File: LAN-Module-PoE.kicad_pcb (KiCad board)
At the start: 2 copper layers, 28.6 x 53.3 mm, 91 parts, among them J1 HY931147C, J10 ProtoCastellatedHeader, J11 ProtoCastellatedHeader, J12 ProtoCastellatedHeader, J13 ProtoCastellatedHeader, J14 ProtoCastellatedHeader, J15 ProtoCastellatedHeader, J16 ProtoCastellatedHeader, J17 ProtoCastellatedHeader, J18 ProtoCastellatedHeader, J19 ProtoCastellatedHeader, J20 ProtoCastellatedHeader, J21 ProtoCastellatedHeader, J22 ProtoCastellatedHeader, J23 ProtoCastellatedHeader, J24 ProtoCastellatedHeader, J25 ProtoCastellatedHeader, J26 ProtoCastellatedHeader, J27 ProtoCastellatedHeader, J28 ProtoCastellatedHeader, J3 ProtoCastellatedHeader, J4 ProtoCastellatedHeader, J5 ProtoCastellatedHeader, J6 ProtoCastellatedHeader, J7 ProtoCastellatedHeader, J8 ProtoCastellatedHeader, J9 ProtoCastellatedHeader, SW1 RESET, U1 ESP32-U4WDH, U2 Si3404, U3 LV2842XLVDDCR, U4 RTL8201F, Y1 40MHz ±10ppm

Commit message: Final revision of PoE variant
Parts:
- added C17: 100n, Capacitor_SMD:C_0603_1608Metric, F.Cu at (41.8, 43.8)
- added D3: Green, LED_SMD:LED_0603_1608Metric, F.Cu at (46.0, 27.5)
- added R26: 33k 1%, Resistor_SMD:R_0603_1608Metric, F.Cu at (39.5, 43.0)
- added R27: 10k 1%, Resistor_SMD:R_0603_1608Metric, F.Cu at (39.5, 44.2)
- added R28: 1k, Resistor_SMD:R_0603_1608Metric, F.Cu at (47.8, 27.5)
- J10, J11, J12, J13, J14, J15, J16, J17, J18, J19, J20, J21, J22, J23, J24, J25, J26, J27, J28, J3, J4, J5, J6, J7, J8, J9: footprint Visclib:ProtoCastellatedHeader_65mil -> Visclib:ProtoHeader_65mil
- L2: value 10uH -> 10uH 1A
- moved SW1 19.7 mm to (27.4, 27.4)
- moved L2 18.7 mm to (44.8, 43.8), turned to 0 degrees
- moved U3 17.1 mm to (40.8, 47.2), turned to -90 degrees
- moved D2 10.9 mm to (44.8, 47.0), turned to 0 degrees
- moved R5 10.1 mm to (26.2, 30.2), turned to 0 degrees
- moved R22 8.41 mm to (41.1, 27.1)
- moved C10 7.36 mm to (26.2, 33.5), turned to 180 degrees
- moved R24 6.50 mm to (37.5, 47.6)
- moved R4 5.13 mm to (42.7, 27.1), turned to -90 degrees
- moved R1 4.72 mm to (26.2, 32.0), turned to 0 degrees
- moved R23 4.37 mm to (37.5, 49.0), turned to 0 degrees
- moved C21 1.63 mm to (45.8, 40.8), turned to 180 degrees
- moved C12 0.50 mm to (40.2, 41.0)
- moved C13 0.25 mm to (43.2, 38.6)
- moved R2 0.20 mm to (30.6, 28.6)
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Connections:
- C1 pad 1: /VIN -> /12V
- C18 pad 1: /VIN -> /12V
- C27 pad 1: /VIN -> /12V
- C4 pad 1: /VIN -> /12V
- D1 pad 1: /VIN -> /12V
- D2 pad 1: unconnected-(D2-Pad1) -> Net-(C17-Pad2)
- D2 pad 2: unconnected-(D2-Pad2) -> GND
- J1 pad 9: /VIN -> /12V
- J1 pad SH: (no net) -> GND
- J15 pad 1: /3V3 -> +3V3
- J28 pad 1: /VIN -> /12V
- L2 pad 1: unconnected-(L2-Pad1) -> Net-(C17-Pad2)
- L2 pad 2: unconnected-(L2-Pad2) -> +3V3
- R19 pad 1: /VIN -> /12V
- R23 pad 2: /VIN -> /12V
- R6 pad 1: /VIN -> /12V
- U2 pad 13: /VIN -> /12V
- U3 pad 1: unconnected-(U3-Pad1) -> Net-(C17-Pad1)
- U3 pad 3: unconnected-(U3-Pad3) -> Net-(R26-Pad1)
- U3 pad 4: unconnected-(U3-Pad4) -> /12V
- U3 pad 5: unconnected-(U3-Pad5) -> /12V
- U3 pad 6: unconnected-(U3-Pad6) -> Net-(C17-Pad2)
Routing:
- net GND: track 116.9 -> 241.5 mm, vias 12 -> 22
- net /12V: track 0.00 -> 61.8 mm, vias 0 -> 2
- net /VIN: track 48.8 -> 0.00 mm, vias 2 -> 0
- net +3V3: track 51.6 -> 95.7 mm, vias 3 -> 5
- net /EN: track 9.56 -> 28.6 mm, vias 1 -> 2
- net /U0RXD: track 1.73 -> 14.0 mm, vias 0 -> 1
- net Net-(R22-Pad2): track 27.1 -> 15.0 mm
- net /BOOT: track 16.3 -> 23.9 mm
- net /POE_NEG: track 29.3 -> 21.8 mm
- net /U0TXD: track 1.76 -> 9.14 mm, vias 0 -> 1
- net Net-(C17-Pad2): track 0.00 -> 7.13 mm
- net /IO13: track 18.1 -> 24.2 mm, vias 1 -> 2
- net /ETH_RXD0: track 25.0 -> 30.9 mm
- net /IO16: track 18.4 -> 24.1 mm, vias 1 -> 2
- net /ETH_RXD1: track 24.4 -> 29.9 mm
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- added copper zone on F.Cu, net +3V3
- added copper zone on F.Cu, net /12V
- added copper zone on F.Cu, net /SWO
- added copper zone on B.Cu, net GND
- added copper zone on F.Cu, net GND
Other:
- board text added: "12V"
- board text added: "3.3V"
- board text added: "BOOT"
- board text added: "EN"
- board text added: "GND"
- board text added: "IO12"
- board text added: "IO13"
- board text added: "IO14"
- board text added: "IO15"
- board text added: "IO16"
- board text added: "IO2"
- board text added: "IO32"
- board text added: "IO33"
- board text added: "IO34"
- board text added: "IO35"
- board text added: "IO37"
- board text added: "IO38"
- board text added: "IO4"
- board text added: "IO5"
- board text added: "RX"
- board text added: "TX"
- board text added: "VN"
- board text added: "VP"

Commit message: Fix footprint for ESP32 (QFN 5x5), add heat pad for PoE regulator
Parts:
- C8: footprint Capacitor_SMD:C_0603_1608Metric -> Resistor_SMD:R_0603_1608Metric
- R23: value 10k -> 1k
- R24: value 10k -> 8.2k
- U1: footprint Visclib:ESP32-REDUCED -> Package_DFN_QFN:QFN-48-1EP_5x5mm_P0.35mm_EP3.7x3.7mm_ThermalVias
- moved L1 0.20 mm to (41.4, 33.6)
- moved C16 0.10 mm to (41.4, 35.1)
- moved U1 0.10 mm to (36.3, 32.0)
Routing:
- net Net-(R4-Pad2): track 18.7 -> 44.1 mm
- net Net-(R22-Pad2): track 15.0 -> 38.3 mm
- net +3V3: track 95.7 -> 104.3 mm, vias 5 -> 10
- net /ETH_RXD1: track 29.9 -> 25.2 mm
- net /IO15: track 22.4 -> 26.5 mm
- net /ETH_RXD0: track 30.9 -> 28.3 mm
- net /EN: track 28.6 -> 30.9 mm
- net /ETH_MDC: track 8.42 -> 10.2 mm, vias 0 -> 2
- net /IO4: track 28.1 -> 29.9 mm
- net /ETH_MDIO: track 9.18 -> 10.9 mm, vias 0 -> 2
- net /IO5: track 29.3 -> 30.8 mm
- net /IO14: track 34.7 -> 36.1 mm
- net /IO35: track 18.1 -> 19.3 mm
- net /IO32: track 16.1 -> 17.2 mm
- net /BOOT: track 23.9 -> 25.0 mm
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- added copper zone on B.Cu, net /POE_NEG
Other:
- board size 28.6 x 53.3 mm -> 28.6 x 53.8 mm

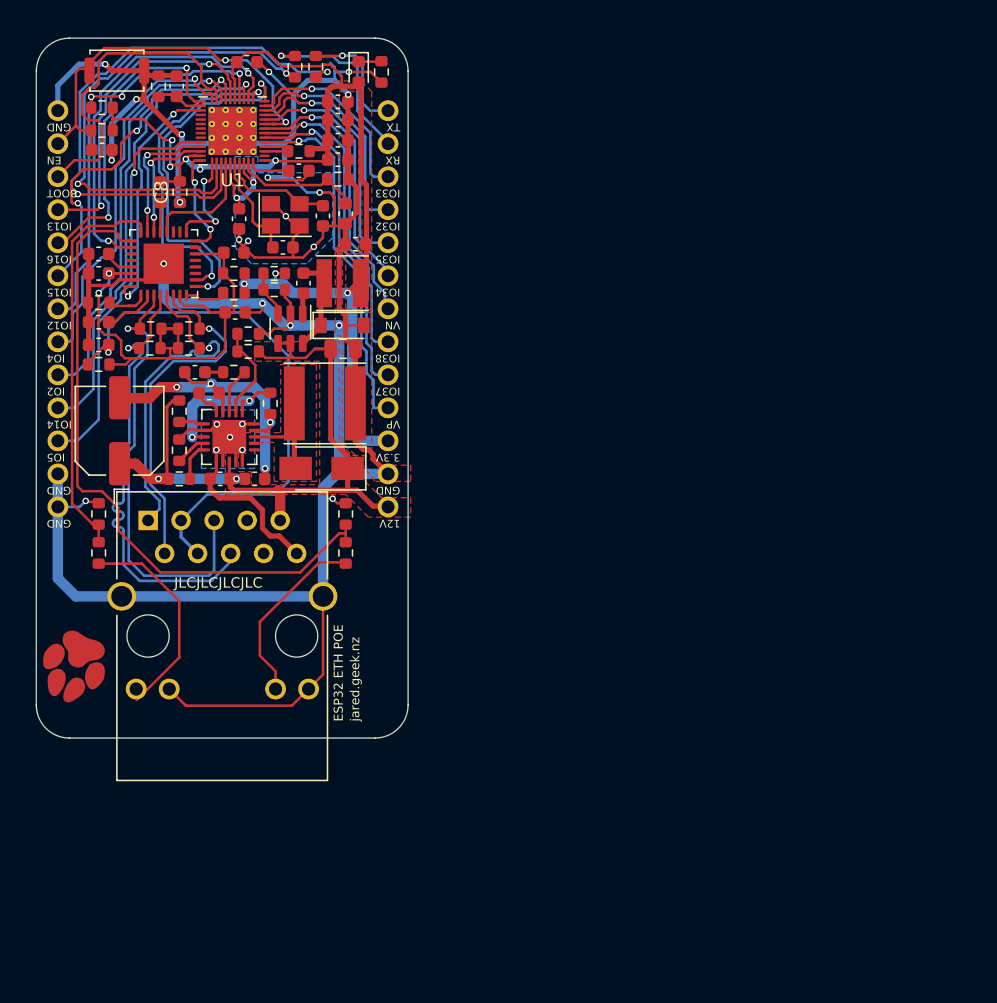
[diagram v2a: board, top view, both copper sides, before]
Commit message: Re-layout with narrower board outline (-0.1")
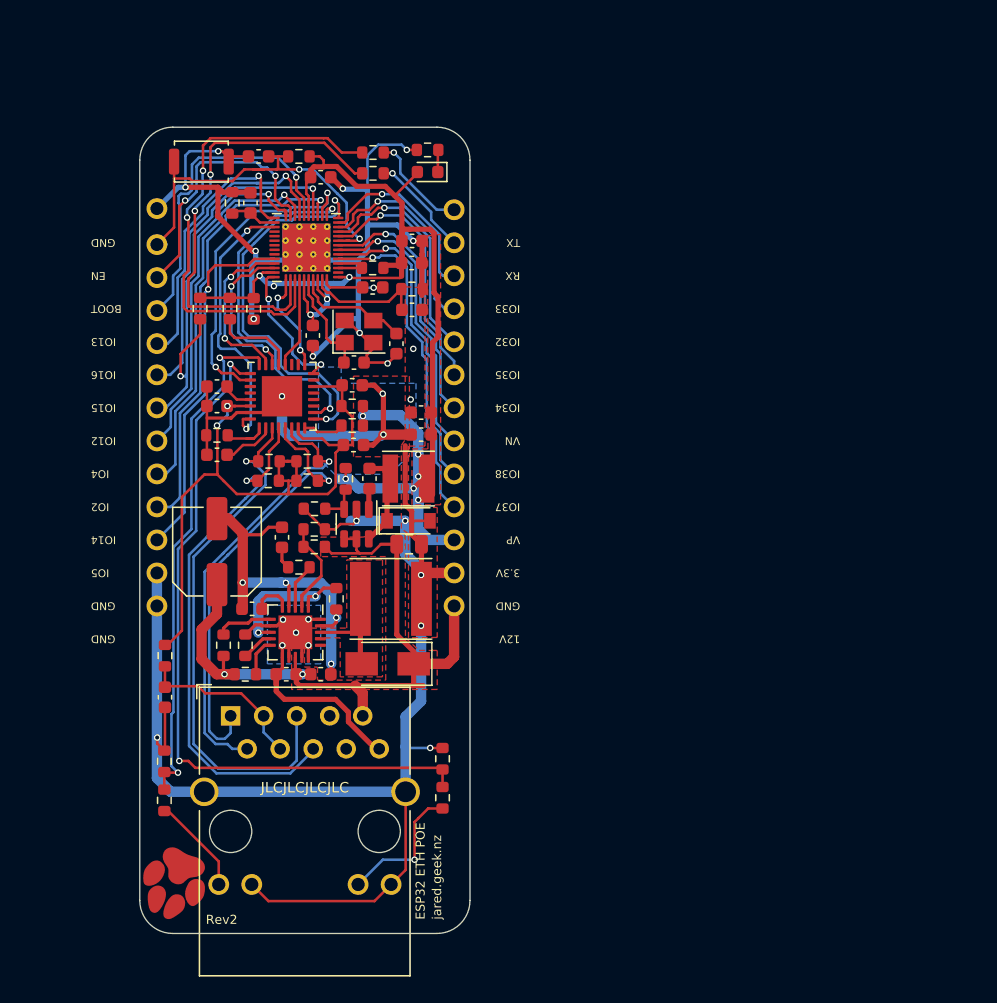
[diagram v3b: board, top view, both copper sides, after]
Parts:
- removed C7: 100n, Capacitor_SMD:C_0603_1608Metric
- moved C3 27.6 mm to (31.1, 75.6), turned to 90 degrees
- moved C5 23.4 mm to (50.8, 53.7), turned to 0 degrees
- moved R25 23.0 mm to (31.1, 72.4), turned to -90 degrees
- moved R11 20.3 mm to (52.5, 80.3)
- moved R16 20.3 mm to (52.5, 83.3)
- moved R12 19.7 mm to (31.1, 80.5)
- moved R15 19.7 mm to (31.1, 83.5)
- moved LOGO1 18.4 mm to (31.7, 90.2)
- moved R6 18.3 mm to (35.6, 71.6), turned to 90 degrees
- moved R5 17.2 mm to (33.8, 45.7), turned to 90 degrees
- moved R27 17.1 mm to (42.6, 61.1), turned to 0 degrees
- moved C20 16.9 mm to (37.8, 68.8), turned to 180 degrees
- moved R26 16.7 mm to (45.0, 58.8), turned to 90 degrees
- moved J1 16.3 mm to (36.1, 77.0)
- moved C1 15.9 mm to (40.4, 73.8)
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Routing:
- net /MDI0_CT: track 42.5 -> 12.9 mm, vias 1 -> 0
- net GND: track 242.0 -> 222.5 mm, vias 20 -> 22
- net /LAN_3P3V: track 41.0 -> 54.4 mm
- net /RTL_LED0: track 30.8 -> 39.9 mm, vias 0 -> 2
- net /ETH_LED0: track 16.4 -> 7.56 mm
- net /MDI1_P: track 26.4 -> 34.6 mm
- net /MDI1_N: track 27.2 -> 34.2 mm
- net Net-(R4-Pad2): track 44.1 -> 37.2 mm
- net /MDI0_P: track 34.6 -> 41.5 mm
- net /MDI0_N: track 35.7 -> 41.2 mm
- net /U0RXD: track 14.0 -> 8.58 mm
- net /RTL_LED1: track 50.6 -> 55.9 mm, vias 0 -> 2
- net /ETH_CRS_DV: track 29.7 -> 25.1 mm
- net /BOOT: track 25.0 -> 20.4 mm, vias 0 -> 2
- net /12V: track 61.8 -> 66.2 mm
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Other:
- board size 28.6 x 53.8 mm -> 25.4 x 62 mm
- board text added: "Rev2"
- board text removed: "USB-UART"

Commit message: Finalize layout for rev2
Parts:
- added C28: 1u, Capacitor_SMD:C_0603_1608Metric, F.Cu at (35.9, 64.4)
- added C7: 1u, Capacitor_SMD:C_0603_1608Metric, F.Cu at (34.4, 64.4)
- added J2: ProtoCastellatedHeader, Visclib:ProtoHeader_65mil, F.Cu at (53.3, 73.7)
- added J29: ProtoCastellatedHeader, Visclib:ProtoHeader_65mil, F.Cu at (53.3, 76.3)
- added L4: 10uH, Inductor_SMD:L_Taiyo-Yuden_NR-80xx, F.Cu at (62.0, 67.7)
- added R29: 50R, Resistor_SMD:R_0603_1608Metric, F.Cu at (45.5, 36.1)
- added R30: 50R, Resistor_SMD:R_0603_1608Metric, F.Cu at (44.0, 36.1)
- added R31: 50R, Resistor_SMD:R_0603_1608Metric, F.Cu at (35.1, 50.2)
- added R32: 50R, Resistor_SMD:R_0603_1608Metric, F.Cu at (37.2, 40.0)
- added TP1: TP, Visclib:TP-1MM, F.Cu at (39.9, 47.6)
- added TP2: TP, Visclib:TP-1MM, F.Cu at (39.4, 67.5)
- C22: footprint Capacitor_SMD:C_0603_1608Metric -> Resistor_SMD:R_0603_1608Metric
- R14, R17, R18: value 49.9R 1% -> 50R 1%
- R20: value 620m -> 1.2R; footprint Resistor_SMD:R_0603_1608Metric -> Resistor_SMD:R_0805_2012Metric
- R7: value 48.7R -> 75R
- Y1: value 40MHz ±10ppm -> 40MHz
- moved C19 2.63 mm to (44.9, 33.7)
- moved R4 1.97 mm to (48.1, 35.4)
- moved R21 1.84 mm to (39.6, 65.2), turned to -90 degrees
- moved R22 1.72 mm to (48.1, 33.9)
- moved R28 1.68 mm to (50.8, 35.1), turned to 90 degrees
- moved D3 1.20 mm to (52.5, 35.1), turned to -90 degrees
- moved C6 1.19 mm to (39.6, 62.2)
- moved C3 0.60 mm to (31.1, 76.2)
- moved R25 0.60 mm to (31.1, 73.0)
- moved R20 0.51 mm to (44.0, 67.6)
- moved R12 0.20 mm to (31.2, 80.4)
- moved R15 0.20 mm to (31.2, 83.4)
- moved R11 0.17 mm to (52.6, 80.4)
- moved R16 0.17 mm to (52.6, 83.4)
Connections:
- U4 pad 10: /ETH_RXD1 -> /RXD1
- U4 pad 26: /ETH_CRS_DV -> /CRS_DV
- U4 pad 32: /ETH_CLK -> Net-(U4-Pad32)
- U4 pad 9: /ETH_RXD0 -> /RXD0
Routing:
- net /RXD0: track 0.00 -> 32.0 mm, vias 0 -> 2
- net /RXD1: track 0.00 -> 29.9 mm, vias 0 -> 2
- net /ETH_RXD0: track 31.2 -> 2.45 mm, vias 2 -> 0
- net /ETH_RXD1: track 28.0 -> 1.93 mm, vias 2 -> 0
- net Net-(U4-Pad32): track 0.00 -> 20.0 mm, vias 0 -> 2
- net /ETH_CLK: track 21.6 -> 1.73 mm, vias 2 -> 0
- net /VIN_NEG: track 11.1 -> 30.7 mm, vias 2 -> 4
- net /ETH_TXD1: track 7.91 -> 13.2 mm
- net /ETH_CRS_DV: track 25.1 -> 20.8 mm
- net Net-(R4-Pad2): track 37.2 -> 40.9 mm, vias 2 -> 4
- net /LAN_3P3V: track 54.4 -> 57.8 mm
- net /ETH_TXD0: track 10.8 -> 14.0 mm
- net /MDI0_N: track 41.2 -> 44.1 mm
- net +3V3: track 107.6 -> 110.2 mm
- net /CRS_DV: track 0.00 -> 2.15 mm
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- removed copper zone on B.Cu, net GND
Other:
- board size 25.4 x 62 mm -> 25.3 x 61 mm
- board text added: "+V"
- board text added: "-V"
- board text added: "AUX"
- board text added: "CLASS"
- board text added: "Class 1 2 3 0"
- board text added: "PMAX 3.8W 6.5W 13W 13W"
- board text added: "R"
- board text added: "RCLASS 140Ω 75Ω 48.7Ω -"
- board text added: "RSNS 2Ω 1.2Ω 0.62Ω 0.62Ω"
- board text added: "RST"
- board text added: "SNS"
- board text added: "WARNING: PoE is +V referenced (VIN = 50V)"

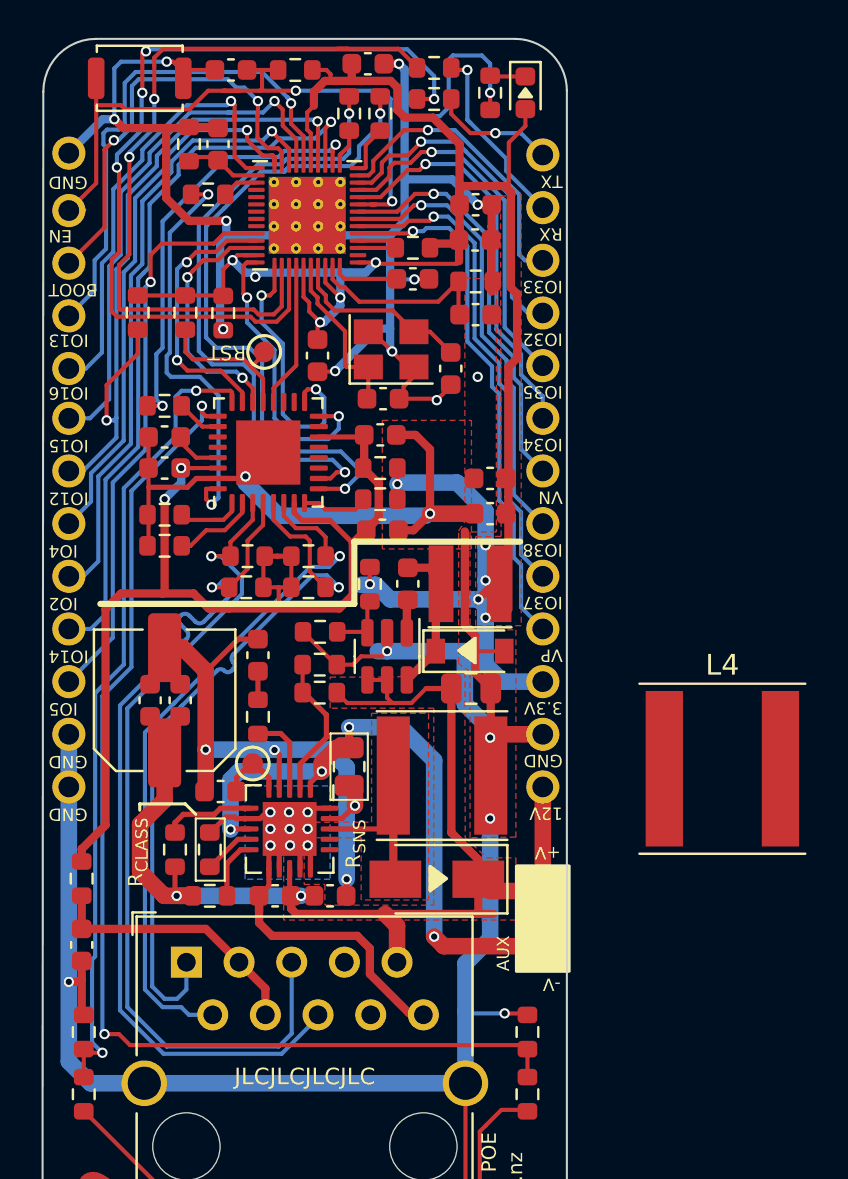
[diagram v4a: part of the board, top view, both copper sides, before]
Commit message: Final PoE design with fixes for rev2 gerber spin
- MTDI must not be pulled high
- GPIO17 for PHY clock conflicts with internal flash
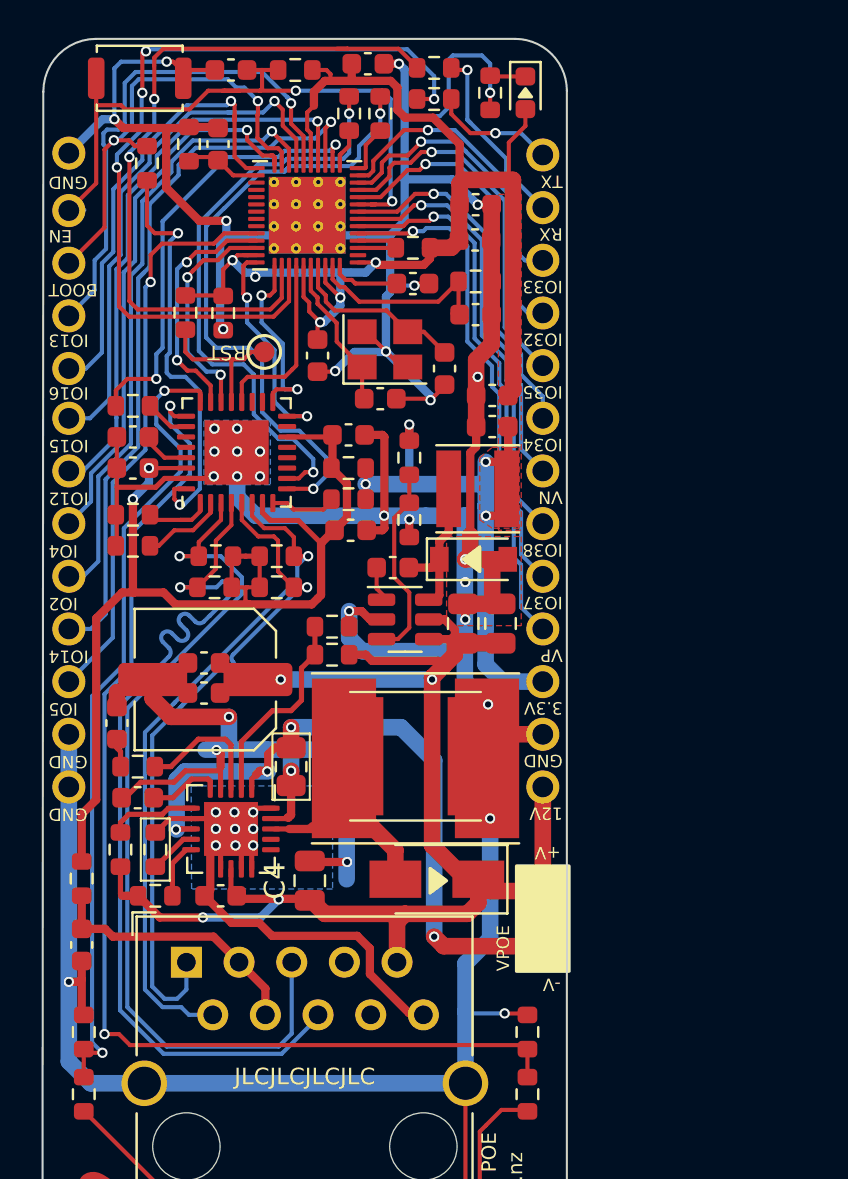
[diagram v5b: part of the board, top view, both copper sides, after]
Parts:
- removed the L4 at (62.0, 67.7)
- removed R5: 10K, Resistor_SMD:R_0603_1608Metric
- removed TP2: TP, Visclib:TP-1MM
- added C29: 2.2u, Capacitor_SMD:C_0805_2012Metric, F.Cu at (49.5, 60.7)
- added L5: -, Inductor_SMD:L_Taiyo-Yuden_NR-60xx, F.Cu at (47.2, 67.1)
- C4: footprint Capacitor_SMD:C_0603_1608Metric -> Capacitor_SMD:C_0805_2012Metric
- L4: value 10uH -> 33uH; footprint Inductor_SMD:L_Taiyo-Yuden_NR-60xx -> Inductor_SMD:L_Taiyo-Yuden_NR-80xx_HandSoldering
- moved C6 7.55 mm to (32.8, 65.5)
- moved R27 6.90 mm to (46.9, 55.7), turned to 90 degrees
- moved R26 6.39 mm to (46.9, 52.7)
- moved R21 6.28 mm to (33.8, 67.6), turned to 0 degrees
- moved L2 4.60 mm to (50.2, 54.2)
- moved D2 4.43 mm to (50.0, 57.6)
- moved C21 4.20 mm to (50.9, 51.2)
- moved C20 4.01 mm to (33.8, 69.1)
- moved C5 4.00 mm to (50.9, 49.7)
- moved C18 3.44 mm to (51.3, 60.7), turned to 90 degrees
- moved R32 3.31 mm to (34.2, 38.5), turned to -90 degrees
- moved U2 2.83 mm to (38.3, 70.6)
- moved R20 2.80 mm to (41.2, 67.6)
- moved C1 2.63 mm to (37.8, 73.8)
- moved R19 2.63 mm to (34.6, 73.8)
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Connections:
- net Net-(U4-Pad32) renamed /ETHCLK
- R32 pad 1: /ETH_CLK -> /BOOT
- U1 pad 27: /ETH_CLK -> unconnected-(U1-Pad27)
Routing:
- net +3V3: track 110.2 -> 95.6 mm, vias 11 -> 9
- net GND: track 224.7 -> 238.9 mm, vias 20 -> 30
- net /POE_NEG: track 23.0 -> 31.5 mm
- net Net-(R26-Pad1): track 3.34 -> 9.24 mm
- net /VSS: track 35.1 -> 40.9 mm
- net /IO12: track 33.5 -> 28.0 mm, vias 2 -> 1
- net /VIN_NEG: track 30.7 -> 35.3 mm
- net /LAN_3P3V: track 57.8 -> 53.6 mm
- net /ETH_TXD1: track 13.2 -> 9.19 mm
- net /ETH_TXD0: track 14.0 -> 10.7 mm
- net /FBH: track 7.04 -> 9.91 mm
- net /COMP: track 3.97 -> 6.47 mm
- net /BOOT: track 20.4 -> 22.8 mm
- net /MDI1_P: track 34.8 -> 32.7 mm
- net /12V: track 67.4 -> 65.4 mm, vias 2 -> 4
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- added copper zone on B.Cu, net GND
- removed copper zone on F.Cu, net /12V
- removed copper zone on F.Cu, net /SWO
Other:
- board text added: "VPOE"
- board text removed: "AUX"
- board text removed: "CLASS"
- board text removed: "R"
- board text removed: "SNS"
